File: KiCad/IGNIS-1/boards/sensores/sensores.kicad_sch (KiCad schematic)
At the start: 12 parts, among them J41 Backplane_2x10, U20 BME280, U21 MPU6050, U22 MQ-135, U24 GPS NEO-6M, U3 Boost_5V

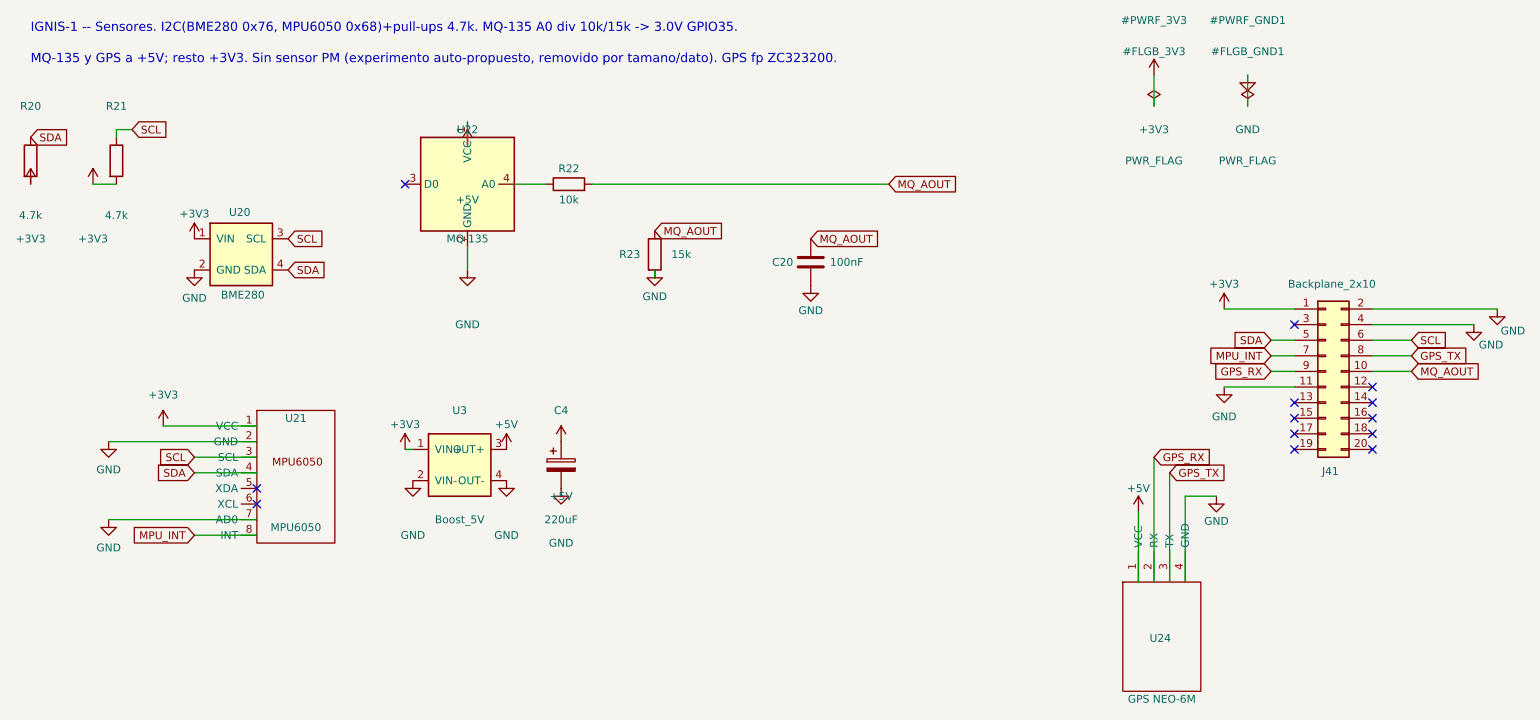
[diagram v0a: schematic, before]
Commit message: Energia: split en 2 boards (carga + energia) y redistribucion de rieles
- Board carga (5º): TP4056 + bateria + RBF + SW1 + TPS63020 -> +3V3 y VSW al bus
- Board energia (4º): MT3608 -> +5V al bus (toma VSW)
- Simbolos nuevos: TP4056, TPS63020; footprints TP4056_HW373, SW_Slide_SS12D00
- Bus: +3V3(p1), +5V(p19), VSW(p20), GND(2/4/11); backplane a header plano
- cerebro: quitada seccion de energia duplicada (U2/J1/J2/SW1/C1), +3V3 del bus
- sensores: quitado MT3608 (U3), +5V del bus alimenta MQ-135/GPS
- ZC323200 eliminado (sin uso)

Co-Authored-By: Claude Opus 4.8 <noreply@anthropic.com>
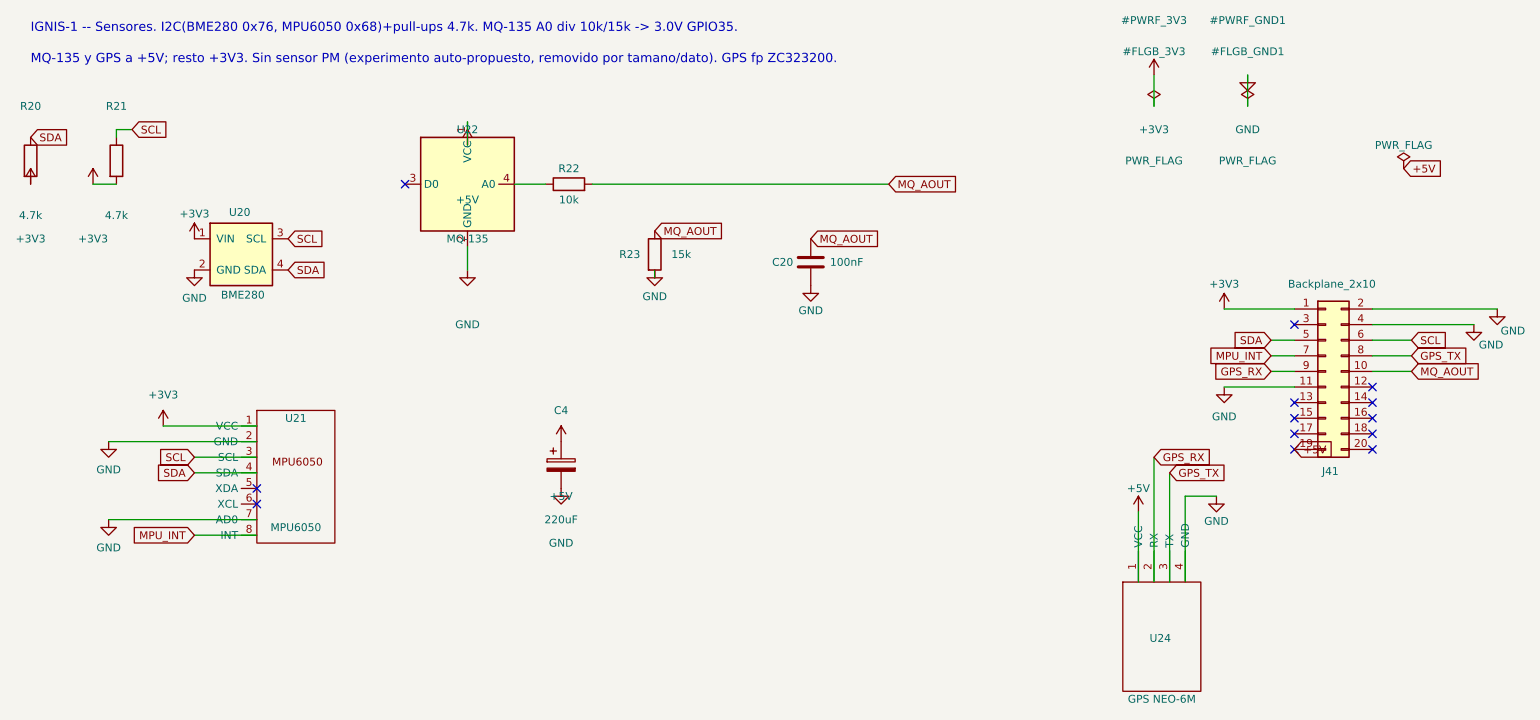
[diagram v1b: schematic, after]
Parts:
- removed U3: Boost_5V, IGNIS1:MT3608_module, symbol IGNIS1:Boost_MT3608
- J41: footprint Connector_IDC:IDC-Header_2x10_P2.54mm_Vertical -> Connector_PinHeader_2.54mm:PinHeader_2x10_P2.54mm_Vertical
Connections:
- net +5V: now also J41.19 (Pin_19)

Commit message: wip: recableo backplane split en progreso (GUI) + doc con move TPS63020
Co-Authored-By: Claude Opus 4.8 <noreply@anthropic.com>
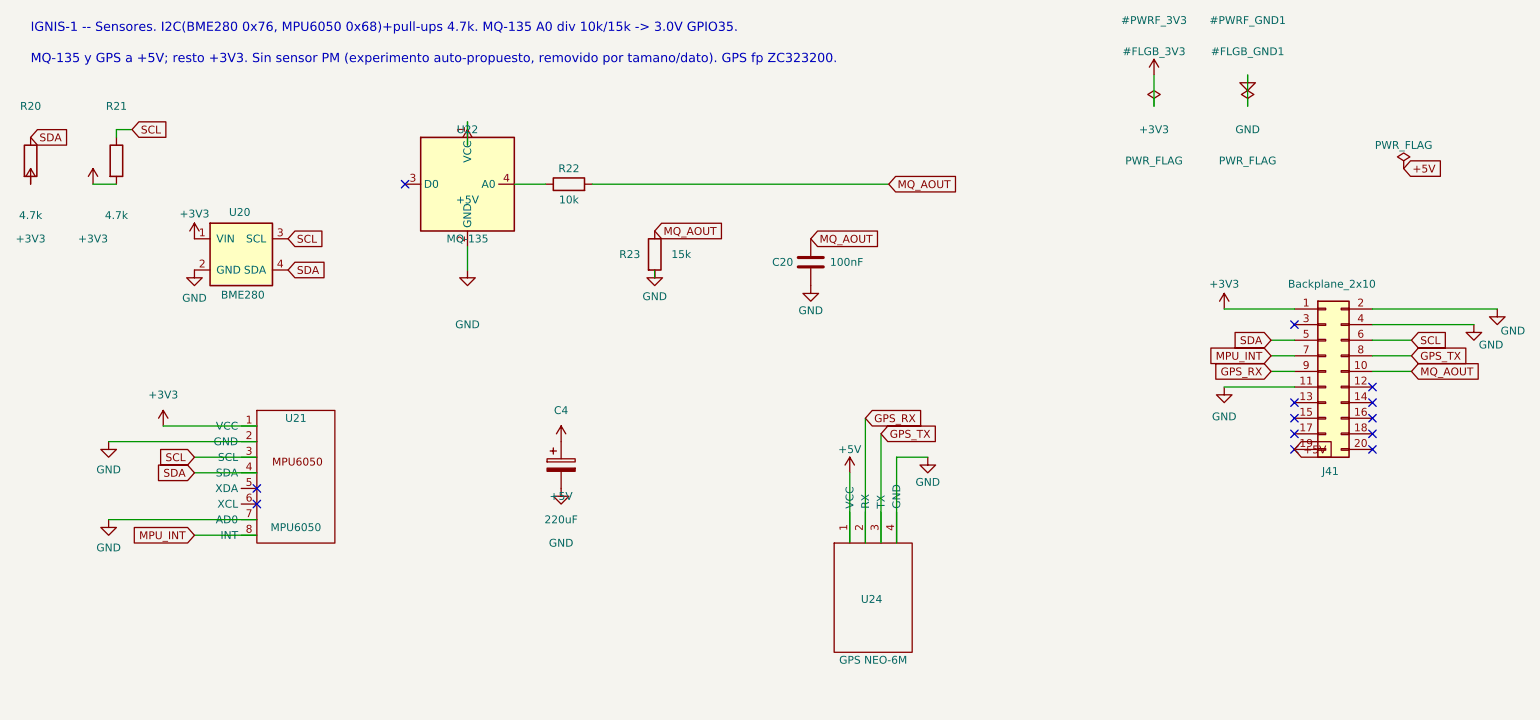
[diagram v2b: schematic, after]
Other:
- moved on the sheet: U24
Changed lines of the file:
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@@
 	(wire
 		(pts
-			(xy 205.74 128.27) (xy 205.74 116.84)
+			(xy 158.75 121.92) (xy 158.75 110.49)
 		)
 		(stroke
@@
 	(wire
 		(pts
-			(xy 210.82 110.49) (xy 210.82 128.27)
+			(xy 163.83 104.14) (xy 163.83 121.92)
 		)
 		(stroke
@@
 		)
 	)
-		(wire
+	(wire
 		(pts
 			(xy 62.23 105.41) (xy 38.1 105.41)
@@
 	(wire
 		(pts
-			(xy 208.28 107.95) (xy 208.28 128.27)
+			(xy 161.29 101.6) (xy 161.29 121.92)
 		)
 		(stroke
@@
 	(wire
 		(pts
-			(xy 218.44 114.3) (xy 213.36 114.3)
+			(xy 171.45 107.95) (xy 166.37 107.95)
 		)
 		(stroke
@@
 	(wire
 		(pts
-			(xy 213.36 114.3) (xy 213.36 128.27)
+			(xy 166.37 107.95) (xy 166.37 121.92)
 		)
 		(stroke
@@
 	(global_label "GPS_TX"
 		(shape input)
-		(at 210.82 110.49 0)
+		(at 163.83 104.14 0)
 		(fields_autoplaced yes)
 		(effects
@@
 		)
 		(property "Intersheetrefs" "${INTERSHEET_REFS}"
-			(at 210.82 110.49 0)
+			(at 163.83 104.14 0)
 			(hide yes)
 			(show_name no)
@@
 		)
 	)
+	(global_label "+5V"
+		(shape input)
+		(at 248.92 60.96 0)
+		(fields_autoplaced yes)
+		(effects
+			(font
+				(size 1.27 1.27)
+			)
+			(justify left)
+		)
+		(property "Intersheetrefs" "${INTERSHEET_REFS}"
+			(at 248.92 60.96 0)
+			(hide yes)
+			(show_name no)
+			(do_not_autoplace no)
+			(effects
+				(font
+					(size 1.27 1.27)
+				)
+			)
+		)
+	)
 	(global_label "MPU_INT"
 		(shape input)
@@
 		)
 	)
+	(global_label "+5V"
+		(shape input)
+		(at 231.14 106.68 0)
+		(fields_autoplaced yes)
+		(effects
+			(font
+				(size 1.27 1.27)
+			)
+			(justify left)
+		)
+		(property "Intersheetrefs" "${INTERSHEET_REFS}"
+			(at 231.14 106.68 0)
+			(hide yes)
+			(show_name no)
+			(do_not_autoplace no)
+			(effects
+				(font
+					(size 1.27 1.27)
+				)
+			)
+		)
+	)
 	(global_label "GPS_RX"
 		(shape input)
-		(at 208.28 107.95 0)
+		(at 161.29 101.6 0)
 		(fields_autoplaced yes)
 		(effects
@@
 		)
 		(property "Intersheetrefs" "${INTERSHEET_REFS}"
-			(at 208.28 107.95 0)
+			(at 161.29 101.6 0)
 			(hide yes)
 			(show_name no)
@@
 		)
 	)
-		(symbol
+	(symbol
 		(lib_id "IGNIS1:MPU6050")
 		(at 68.58 110.49 0)
@@
 		)
 	)
-		(symbol
+	(symbol
 		(lib_id "power:GND")
 		(at 127 77.47 0)
@@
 	(symbol
 		(lib_id "IGNIS1:GPS6MV2")
-		(at 209.55 137.16 0)
+		(at 162.56 130.81 0)
 		(unit 1)
 		(body_style 1)
@@
 		(dnp no)
 		(property "Reference" "U24"
-			(at 209.296 137.414 0)
+			(at 162.306 131.064 0)
 			(show_name no)
 			(do_not_autoplace no)
@@
 		)
 		(property "Value" "GPS NEO-6M"
-			(at 209.55 147.32 0)
+			(at 162.56 140.97 0)
 			(show_name no)
 			(do_not_autoplace no)
@@
 		)
 		(property "Footprint" "IGNIS1:GPS_NEO6M_module"
-			(at 209.55 137.16 0)
+			(at 162.56 130.81 0)
 			(hide yes)
 			(show_name no)
@@
 		)
 		(property "Datasheet" "~"
-			(at 209.55 137.16 0)
+			(at 162.56 130.81 0)
 			(hide yes)
 			(show_name no)
@@
 		)
 		(property "Description" ""
-			(at 209.55 137.16 0)
+			(at 162.56 130.81 0)
 			(show_name no)
 			(do_not_autoplace no)
@@
 		)
 	)
-		(symbol
+	(symbol
 		(lib_id "power:+3V3")
 		(at 35.56 63.5 0)
@@
 	)
 	(symbol
+		(lib_id "power:PWR_FLAG")
+		(at 248.92 60.96 0)
+		(unit 1)
+		(body_style 1)
+		(exclude_from_sim no)
+		(in_bom yes)
+		(on_board yes)
+		(in_pos_files yes)
+		(dnp no)
+		(property "Reference" "#FLGX1"
+			(at 248.92 64.76 0)
+			(hide yes)
+			(show_name no)
+			(do_not_autoplace no)
+			(effects
+				(font
+					(size 1.27 1.27)
+				)
+			)
+		)
+		(property "Value" "PWR_FLAG"
+			(at 248.92 57.16 0)
+			(show_name no)
+			(do_not_autoplace no)
+			(effects
+				(font
+					(size 1.27 1.27)
+				)
+			)
+		)
+		(property "Footprint" ""
+			(at 248.92 60.96 0)
+			(hide yes)
+			(show_name no)
+			(do_not_autoplace no)
+			(effects
+				(font
+					(size 1.27 1.27)
+				)
+			)
+		)
+		(property "Datasheet" "~"
+			(at 248.92 60.96 0)
+			(hide yes)
+			(show_name no)
+			(do_not_autoplace no)
+			(effects
+				(font
+					(size 1.27 1.27)
+				)
+			)
+		)
+		(property "Description" ""
+			(at 248.92 60.96 0)
+			(show_name no)
+			(do_not_autoplace no)
+			(effects
+				(font
+					(size 1.27 1.27)
+				)
+			)
+		)
+		(pin "1"
+		)
+		(instances
+			(project "sensores"
+				(path "/74f32100-bf0b-42ea-8f65-2ce920f7760a"
+					(reference "#FLGX1")
+					(unit 1)
+				)
+			)
+		)
+	)
+	(symbol
 		(lib_id "power:GND")
 		(at 264.16 83.82 0)
@@
 		)
 	)
-			(symbol
+	(symbol
 		(lib_id "power:+5V")
-		(at 205.74 116.84 0)
+		(at 158.75 110.49 0)
 		(unit 1)
 		(body_style 1)
@@
 		(dnp no)
 		(property "Reference" "#PWR_S8"
-			(at 205.74 107.95 0)
+			(at 158.75 101.6 0)
 			(hide yes)
 			(show_name no)
@@
 		)
 		(property "Value" "+5V"
-			(at 205.74 113.03 0)
+			(at 158.75 106.68 0)
 			(show_name no)
 			(do_not_autoplace no)
@@
 		)
 		(property "Footprint" ""
-			(at 205.74 116.84 0)
+			(at 158.75 110.49 0)
 			(hide yes)
 			(show_name no)
@@
 		)
 		(property "Datasheet" "~"
-			(at 205.74 116.84 0)
+			(at 158.75 110.49 0)
 			(hide yes)
 			(show_name no)
@@
 		)
 		(property "Description" ""
-			(at 205.74 116.84 0)
+			(at 158.75 110.49 0)
 			(show_name no)
 			(do_not_autoplace no)
@@
 	(symbol
 		(lib_id "power:GND")
-		(at 218.44 114.3 0)
+		(at 171.45 107.95 0)
 		(unit 1)
 		(body_style 1)
@@
 		(dnp no)
 		(property "Reference" "#PWR_S9"
-			(at 218.44 105.41 0)
+			(at 171.45 99.06 0)
 			(hide yes)
 			(show_name no)
@@
 		)
 		(property "Value" "GND"
-			(at 218.44 118.364 0)
+			(at 171.45 112.014 0)
 			(show_name no)
 			(do_not_autoplace no)
@@
 		)
 		(property "Footprint" ""
-			(at 218.44 114.3 0)
+			(at 171.45 107.95 0)
 			(hide yes)
 			(show_name no)
@@
 		)
 		(property "Datasheet" "~"
-			(at 218.44 114.3 0)
+			(at 171.45 107.95 0)
 			(hide yes)
 			(show_name no)
@@
 		)
 		(property "Description" ""
-			(at 218.44 114.3 0)
+			(at 171.45 107.95 0)
 			(show_name no)
 			(do_not_autoplace no)
@@
 		)
 	)
-	(symbol
-		(lib_id "power:PWR_FLAG")
-		(at 248.92 60.96 0)
-		(unit 1)
-		(exclude_from_sim no)(in_bom yes)(on_board yes)(dnp no)
-		(property "Reference" "#FLGX1" (at 248.92 64.76 0) (hide yes) (effects (font (size 1.27 1.27))))
-		(property "Value" "PWR_FLAG" (at 248.92 57.160000000000004 0) (effects (font (size 1.27 1.27))))
-		(property "Footprint" "" (at 248.92 60.96 0) (hide yes) (effects (font (size 1.27 1.27))))
-		(property "Datasheet" "~" (at 248.92 60.96 0) (hide yes) (effects (font (size 1.27 1.27))))
-		(pin "1")
-		(instances (project "sensores" (path "/74f32100-bf0b-42ea-8f65-2ce920f7760a" (reference "#FLGX1") (unit 1))))
-	)
-	(global_label "+5V" (shape input) (at 248.92 60.96 0) (fields_autoplaced yes)
-		(effects (font (size 1.27 1.27)) (justify left))
-		(property "Intersheetrefs" "${INTERSHEET_REFS}" (at 248.92 60.96 0) (hide yes) (effects (font (size 1.27 1.27)))))
-	(global_label "+5V" (shape input) (at 231.14 106.68 0) (fields_autoplaced yes)
-		(effects (font (size 1.27 1.27)) (justify left))
-		(property "Intersheetrefs" "${INTERSHEET_REFS}" (at 231.14 106.68 0) (hide yes) (effects (font (size 1.27 1.27)))))
 	(sheet_instances
 		(path "/"
